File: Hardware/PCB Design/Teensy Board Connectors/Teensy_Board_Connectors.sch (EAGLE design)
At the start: 12 parts

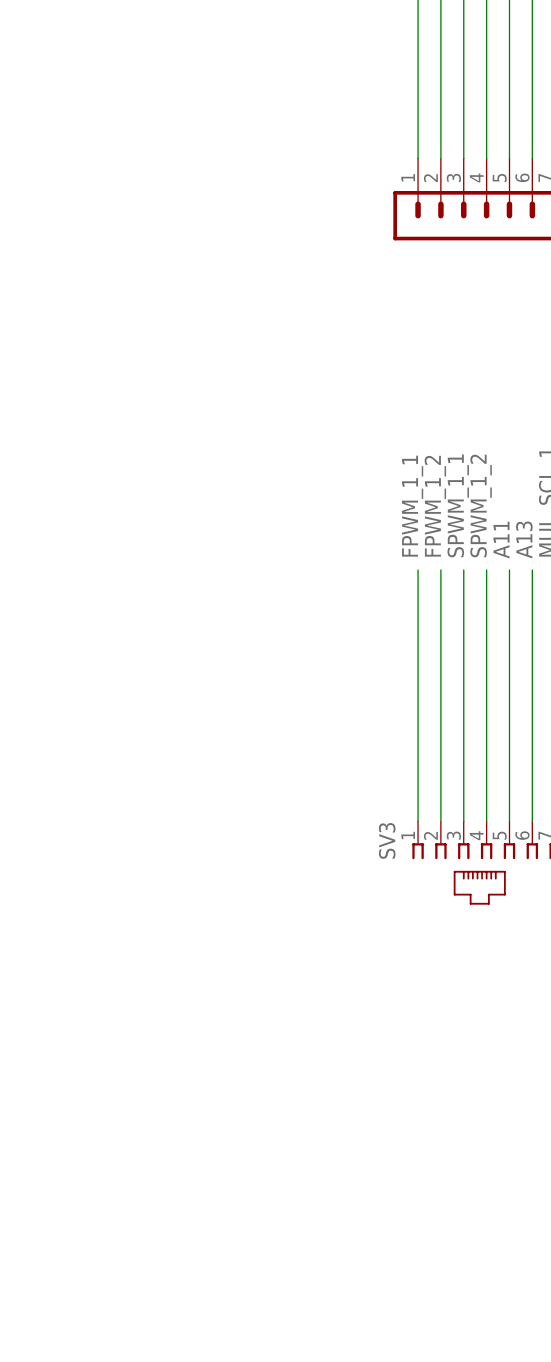
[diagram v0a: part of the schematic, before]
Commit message: Added ULN2803 with SOP18 PKG for the connector board
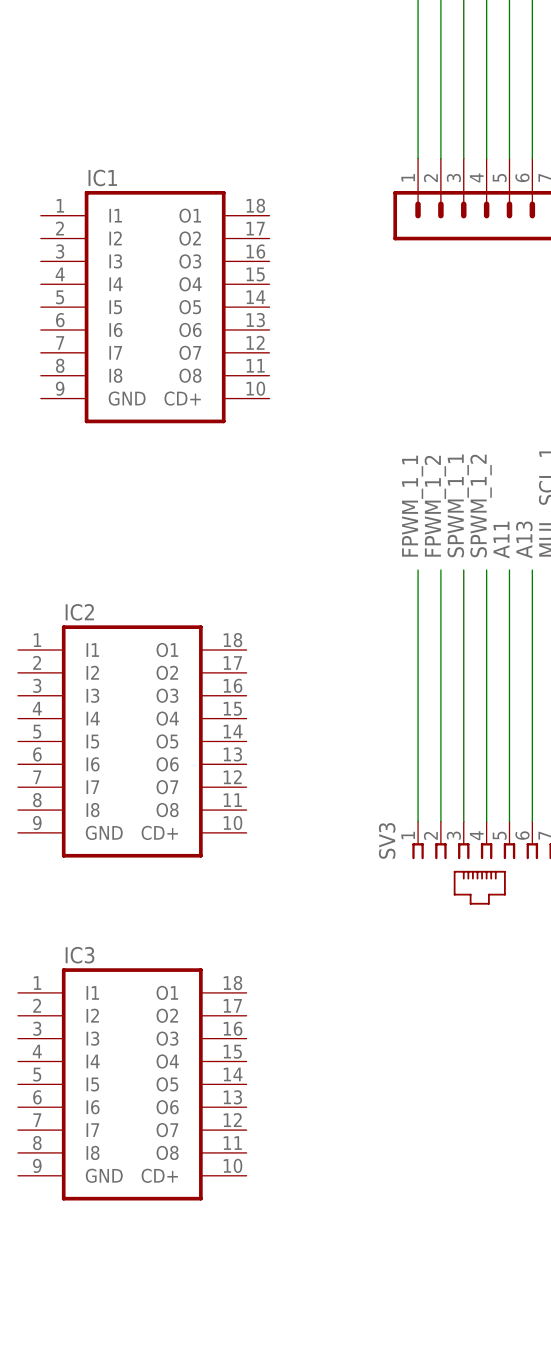
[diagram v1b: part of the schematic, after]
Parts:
- added IC1, IC2, IC3: (no value), CBLA_Test_bed_Library:ULN2803AFWG
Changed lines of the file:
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@@
 <part name="SV11" library="con-lstb" deviceset="MA08-1" device=""/>
 <part name="SV12" library="con-lstb" deviceset="MA08-1" device=""/>
+<part name="IC1" library="CBLA_Test_bed_Library" deviceset="ULN2803A" device="FWG"/>
+<part name="IC2" library="CBLA_Test_bed_Library" deviceset="ULN2803A" device="FWG"/>
+<part name="IC3" library="CBLA_Test_bed_Library" deviceset="ULN2803A" device="FWG"/>
 </parts>
 <sheets>
@@
 <instance part="SV11" gate="1" x="189.23" y="138.43" rot="MR90"/>
 <instance part="SV12" gate="1" x="217.17" y="138.43" rot="MR90"/>
+<instance part="IC1" gate="G$1" x="40.64" y="129.54"/>
+<instance part="IC2" gate="G$1" x="38.1" y="81.28"/>
+<instance part="IC3" gate="G$1" x="38.1" y="43.18"/>
 </instances>
 <busses>

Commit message: Updated signal LEDS
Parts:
- added LED1, LED10, LED11, LED12, LED13, LED14, LED15, LED16, LED17, LED18, LED19, LED2, LED20, LED21, LED22, LED23, LED24, LED3, LED4, LED5, LED6, LED7, LED8, LED9: (no value), led:LEDSML1206
- added R1, R10, R11, R12, R13, R14, R15, R16, R17, R18, R19, R2, R20, R21, R22, R23, R24, R3, R4, R5, R6, R7, R8, R9: 470, CBLA_Test_bed_Library:R-US_R0603
- added X1: (no value), CBLA_Test_bed_Library:PINHD-1X2
- added X2: (no value), CBLA_Test_bed_Library:PINHD-1X3
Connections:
- new net +5V: LED1.A, LED10.A, LED11.A, LED12.A, LED13.A, LED14.A, LED15.A, LED16.A, LED17.A, LED18.A, LED19.A, LED2.A, LED20.A, LED21.A, LED22.A, LED23.A, LED24.A, LED3.A, LED4.A, LED5.A, LED6.A, LED7.A, LED8.A, LED9.A, X2.2
- new net +5VJUMP: X1.1, X2.1
- new net GND: IC1.GND, IC2.GND, IC3.GND, X1.2
- new net N$1: IC1.O1, R1.1
- new net N$10: IC1.O8, R8.1
- new net N$11: LED2.C, R2.2
- new net N$12: LED3.C, R3.2
- new net N$13: LED4.C, R4.2
- new net N$14: LED5.C, R5.2
- new net N$15: LED6.C, R6.2
- new net N$16: LED7.C, R7.2
- new net N$17: LED8.C, R8.2
- new net N$18: IC2.O1, R9.1
- new net N$19: LED9.C, R9.2
- new net N$2: LED1.C, R1.2
- new net N$20: IC2.O2, R10.1
- new net N$21: IC2.O3, R11.1
- new net N$22: IC2.O4, R12.1
- new net N$23: IC2.O5, R13.1
- new net N$24: IC2.O6, R14.1
- new net N$25: IC2.O7, R15.1
- new net N$26: IC2.O8, R16.1
- new net N$27: LED10.C, R10.2
- new net N$28: LED11.C, R11.2
- new net N$29: LED12.C, R12.2
- new net N$3: IC1.O2, R2.1
- new net N$30: LED13.C, R13.2
- new net N$31: LED14.C, R14.2
- new net N$32: LED15.C, R15.2
- new net N$33: LED16.C, R16.2
- new net N$34: IC3.O1, R17.1
- new net N$35: LED17.C, R17.2
- new net N$36: IC3.O2, R18.1
- new net N$37: IC3.O3, R19.1
- new net N$38: IC3.O4, R20.1
- new net N$39: IC3.O5, R21.1
- new net N$4: IC1.O3, R3.1
- new net N$40: IC3.O6, R22.1
- new net N$41: IC3.O7, R23.1
- new net N$42: IC3.O8, R24.1
- new net N$43: LED18.C, R18.2
- new net N$44: LED19.C, R19.2
- new net N$45: LED20.C, R20.2
- new net N$46: LED21.C, R21.2
- new net N$47: LED22.C, R22.2
- new net N$48: LED23.C, R23.2
- new net N$49: LED24.C, R24.2
- new net N$5: IC1.O4, R4.1
- new net N$6: IC1.O5, R5.1
- new net N$7: IC1.O6, R6.1
- new net N$8: IC1.O7, R7.1
- net FPWM_1_1: now also IC1.I1
- net FPWM_1_2: now also IC1.I2
- net FPWM_2_1: now also IC2.I1
- net FPWM_2_2: now also IC2.I2
- net FPWM_4_1: now also IC1.I5
- net FPWM_4_2: now also IC1.I6
- net FPWM_5_1: now also IC2.I5
- net FPWM_5_2: now also IC2.I6
- net SPWM_1_1: now also IC1.I3
- net SPWM_1_2: now also IC1.I4
- net SPWM_2_1: now also IC2.I3
- net SPWM_2_2: now also IC2.I4
- net SPWM_3_1: now also IC3.I1
- net SPWM_3_2: now also IC3.I2
- net SPWM_3_3: now also IC3.I3
- net SPWM_3_4: now also IC3.I4
- net SPWM_4_1: now also IC1.I7
- net SPWM_4_2: now also IC1.I8
- net SPWM_5_1: now also IC2.I7
- net SPWM_5_2: now also IC2.I8
- net SPWM_6_1: now also IC3.I5
- net SPWM_6_2: now also IC3.I6
- net SPWM_6_3: now also IC3.I7
- net SPWM_6_4: now also IC3.I8
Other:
- moved on the sheet: IC1, IC2, IC3, SV1, SV10, SV11, SV12, SV2, SV3, SV4, SV5, SV6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

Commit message: Updated Teensy Board and Connector Board design
- fixed broken connection
- makes everything 45 degrees bend
- moved the RJ45 connectors a bit to the right so they don't interfere
with the power header
- connect common pin to _5V
- added power and ground pour
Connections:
- net +5V: now also IC1.CD+, IC2.CD+, IC3.CD+
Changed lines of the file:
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@@
 <?xml version="1.0" encoding="utf-8"?>
 <!DOCTYPE eagle SYSTEM "eagle.dtd">
-<eagle version="7.0.0">
+<eagle version="7.1.0">
 <drawing>
 <settings>
@@
 <wire x1="91.44" y1="144.78" x2="91.44" y2="142.24" width="0.1524" layer="91"/>
 <junction x="91.44" y="144.78"/>
+<pinref part="IC1" gate="G$1" pin="CD+"/>
+<wire x1="66.04" y1="139.7" x2="91.44" y2="139.7" width="0.1524" layer="91"/>
+<wire x1="91.44" y1="139.7" x2="91.44" y2="142.24" width="0.1524" layer="91"/>
+<junction x="91.44" y="142.24"/>
 </segment>
 <segment>
@@
 <wire x1="91.44" y1="106.68" x2="91.44" y2="104.14" width="0.1524" layer="91"/>
 <junction x="91.44" y="106.68"/>
+<pinref part="IC2" gate="G$1" pin="CD+"/>
+<wire x1="66.04" y1="101.6" x2="91.44" y2="101.6" width="0.1524" layer="91"/>
+<wire x1="91.44" y1="101.6" x2="91.44" y2="104.14" width="0.1524" layer="91"/>
+<junction x="91.44" y="104.14"/>
 </segment>
 <segment>
@@
 <wire x1="91.44" y1="68.58" x2="91.44" y2="66.04" width="0.1524" layer="91"/>
 <junction x="91.44" y="68.58"/>
-</segment>
-<segment>
+<pinref part="IC3" gate="G$1" pin="CD+"/>
+<wire x1="66.04" y1="63.5" x2="91.44" y2="63.5" width="0.1524" layer="91"/>
+<wire x1="91.44" y1="63.5" x2="91.44" y2="66.04" width="0.1524" layer="91"/>
+<junction x="91.44" y="66.04"/>
+</segment>
+<segment>
